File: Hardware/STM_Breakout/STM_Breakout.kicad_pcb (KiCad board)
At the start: 2 copper layers, 30.5 x 30.5 mm, 21 parts, among them J1 Conn_01x12_Pin, SW1 SW_Push, U1 STM32F042F6Px, U2 ATA6561

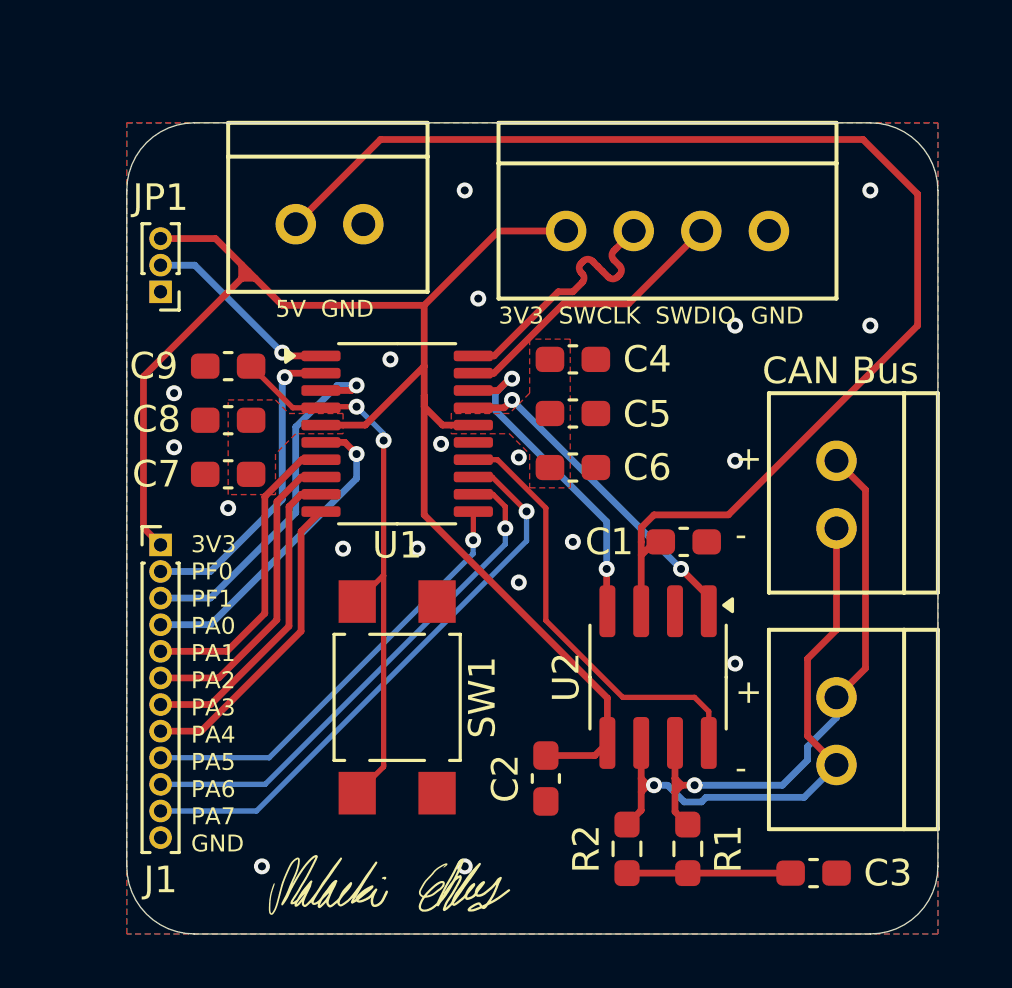
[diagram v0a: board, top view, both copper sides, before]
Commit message: Increase header pitch in STM32 breakout
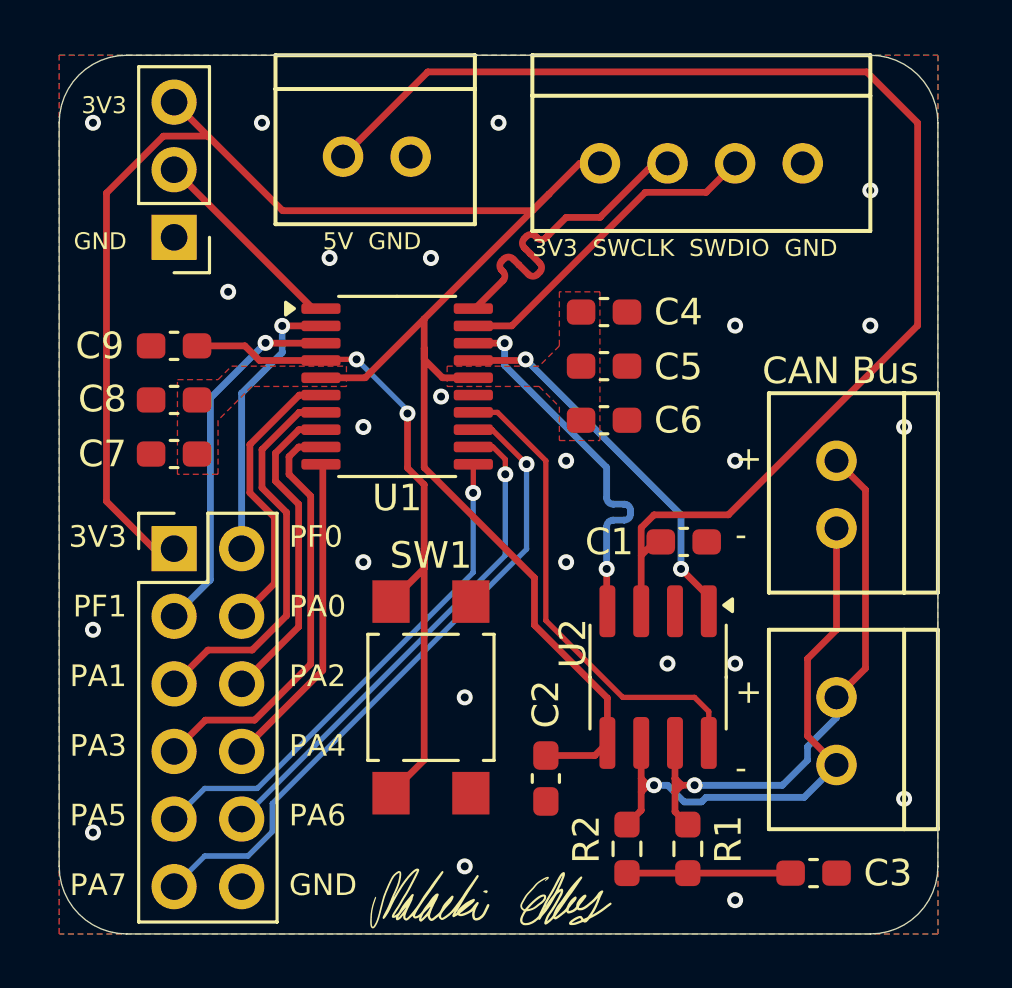
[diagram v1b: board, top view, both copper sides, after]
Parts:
- J1: footprint Connector_PinHeader_1.00mm:PinHeader_1x12_P1.00mm_Vertical -> Connector_PinHeader_2.54mm:PinHeader_2x06_P2.54mm_Vertical
- JP1: footprint Connector_PinHeader_1.00mm:PinHeader_1x03_P1.00mm_Vertical -> Connector_PinHeader_2.54mm:PinHeader_1x03_P2.54mm_Vertical
- moved G*** 3.84 mm to (82.3, 77.5)
- moved Conn2 3.10 mm to (76.7, 49.5)
- moved Conn1 2.84 mm to (86.4, 49.8)
- moved C7 2.17 mm to (70.4, 60.7)
- moved C8 2.17 mm to (70.4, 58.7)
- moved C9 2.17 mm to (70.4, 56.6)
- moved C4 2.13 mm to (86.5, 55.4)
- moved C5 2.13 mm to (86.5, 57.4)
- moved C6 2.13 mm to (86.5, 59.4)
- moved JP1 2.11 mm to (70.4, 52.6)
- moved U1 1.78 mm to (78.7, 58.2)
- moved SW1 1.27 mm to (80.0, 69.8)
- moved J1 0.53 mm to (70.4, 64.3)
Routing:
- net +3V3: track 59.8 -> 73.3 mm
- net /NRST: track 21.4 -> 26.6 mm
- net PA3: track 11.9 -> 16.0 mm
- net PA7: track 21.6 -> 24.9 mm
- net PA1: track 11.6 -> 14.7 mm
- net PA5: track 16.5 -> 19.1 mm
- net SWCLK: track 9.95 -> 12.4 mm
- net STBY: track 16.4 -> 18.2 mm
- net CAN_RX: track 12.4 -> 14.2 mm
- net CAN_TX: track 12.6 -> 14.3 mm
- net SWDIO: track 10.8 -> 12.4 mm
- net PF0: track 11.8 -> 10.5 mm
- net PA0: track 12.1 -> 10.8 mm, vias 1 -> 0
- net +5V: track 48.1 -> 48.9 mm
- net /BOOT0: track 7.44 -> 7.68 mm, vias 1 -> 0
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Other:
- board size 30.5 x 30.5 mm -> 33 x 33 mm
- board text added: "3V3 GND"
- board text added: "3V3 PF1 PA1 PA3 PA5 PA7"
- board text added: "PF0 PA0 PA2 PA4 PA6 GND"
- board text removed: "3V3 PF0 PF1 PA0 PA1 PA2 PA3 PA4 PA5 PA6 PA7 GND"

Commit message: Replace reset button with jumper
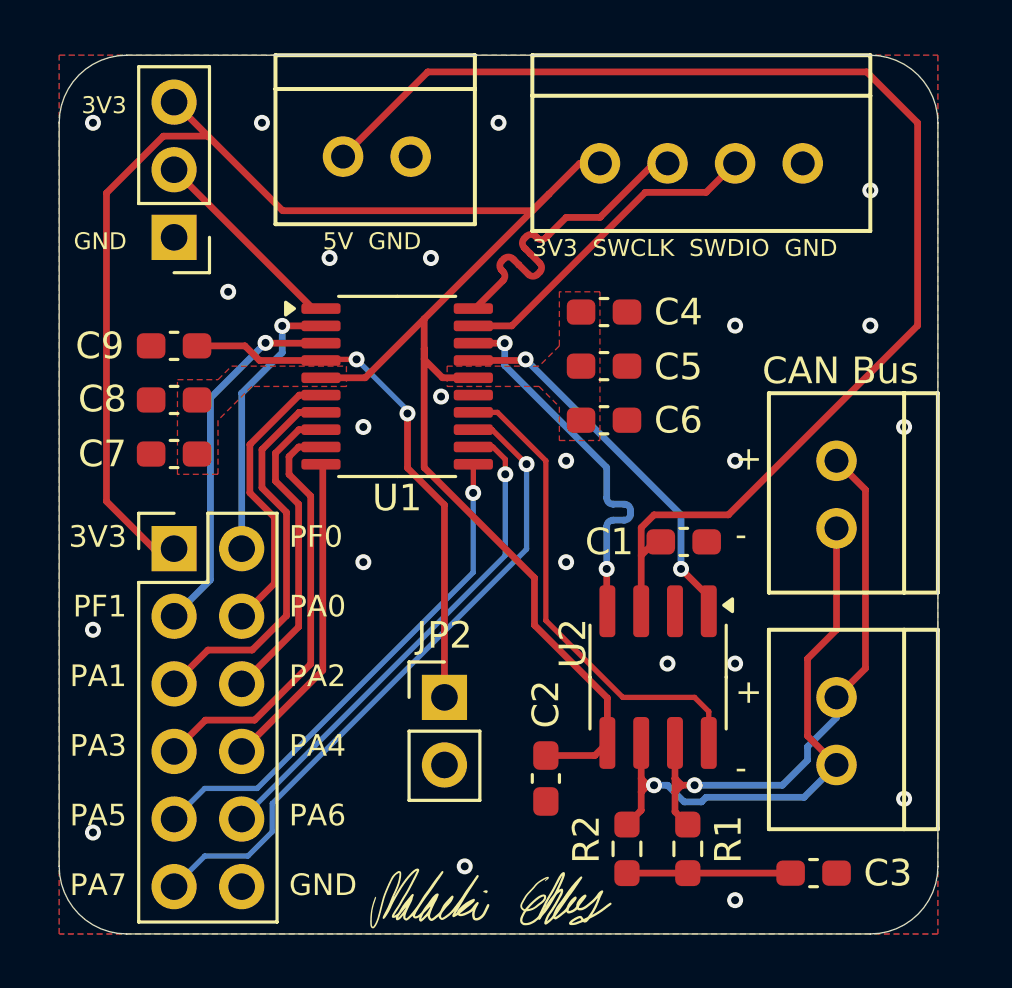
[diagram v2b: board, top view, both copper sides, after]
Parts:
- removed SW1: SW_Push, Button_Switch_SMD:SW_SPST_TL3305A
- added JP2: Jumper_2_Open, Connector_PinHeader_2.54mm:PinHeader_1x02_P2.54mm_Vertical, F.Cu at (80.5, 69.8)
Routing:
- net /NRST: track 26.6 -> 20.3 mm
- net GND: vias 24 -> 23
